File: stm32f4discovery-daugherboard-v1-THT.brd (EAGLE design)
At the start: 100 x 70 mm, 44 parts

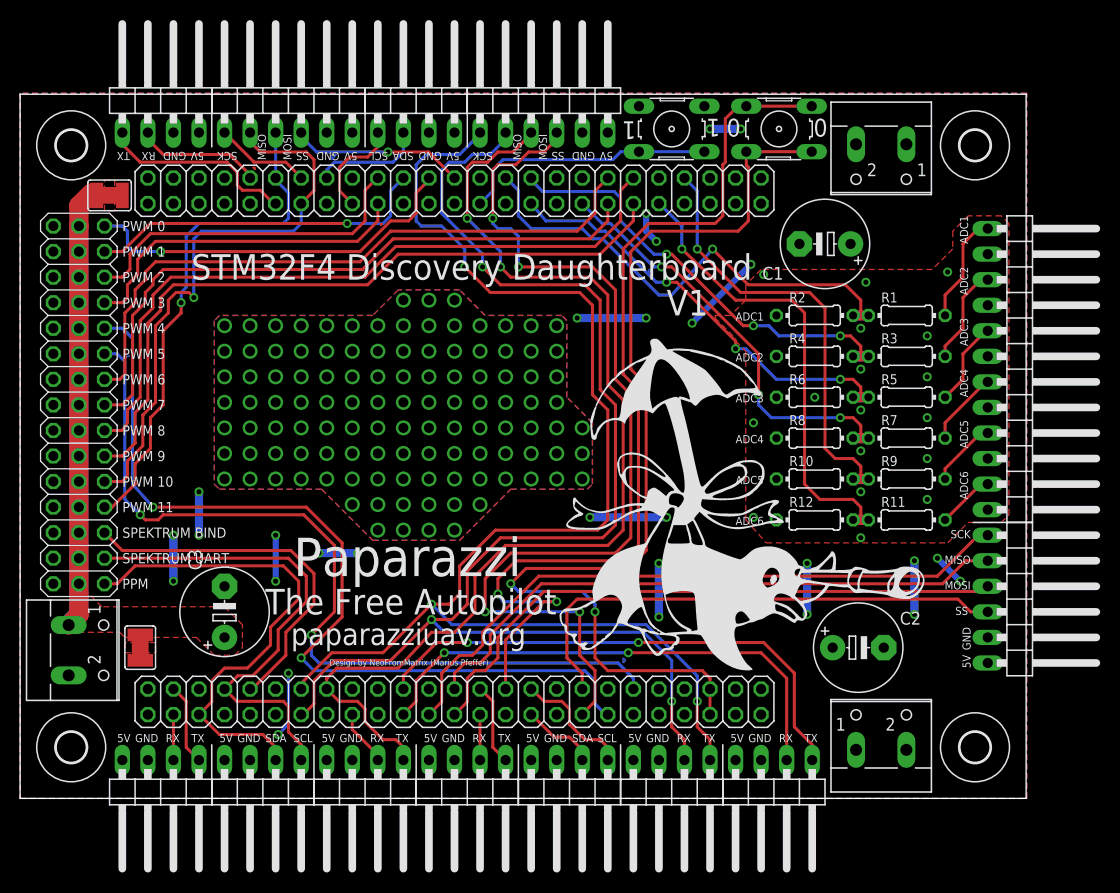
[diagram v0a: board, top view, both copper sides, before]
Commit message: all tht components, adc input protection with diodes
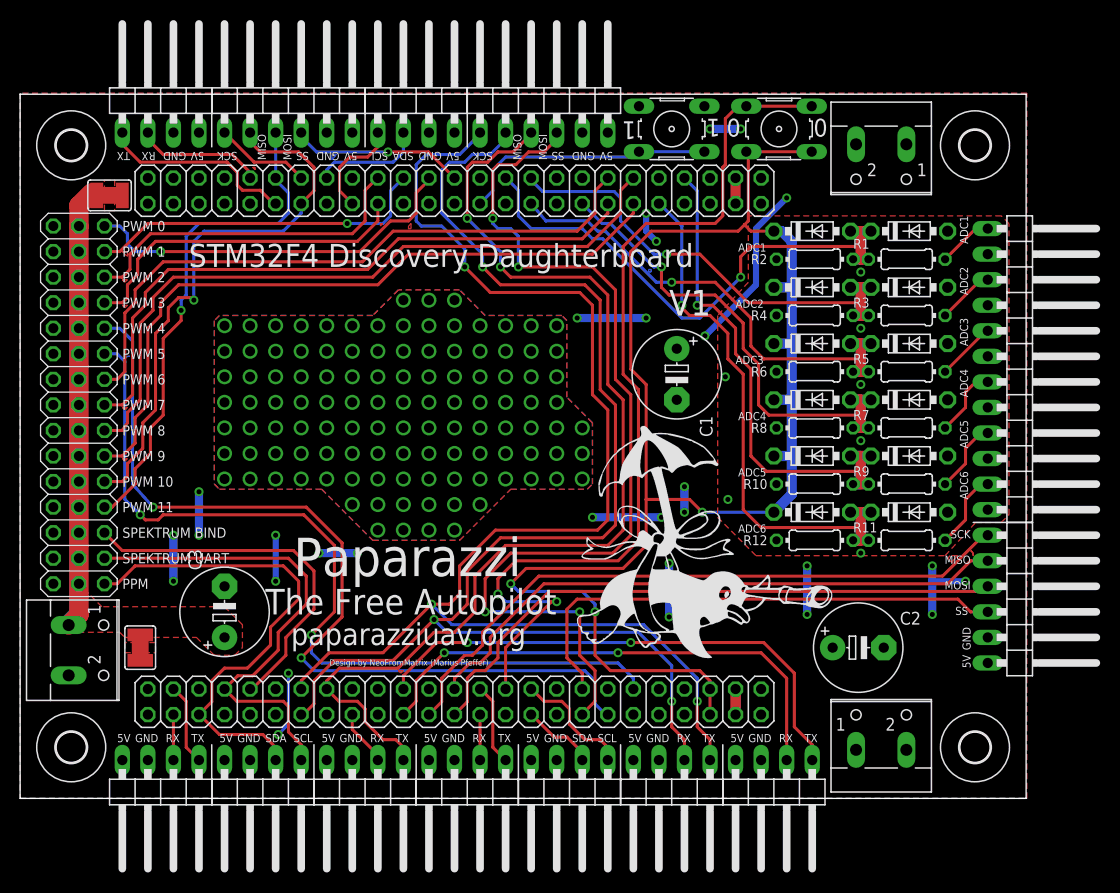
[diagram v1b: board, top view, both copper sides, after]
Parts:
- removed U$3: PAPARAZZI, paparazzi:PAPARAZZI
- added D1, D10, D11, D12, D2, D3, D4, D5, D6, D7, D8, D9: 1N4007, diode:DO41-7.6_2
- added U$4: üAüARAZZI_1400, paparazzi:PAPARAZZI_1400
- moved C1 19.6 mm to (65.3, 42.2), turned to 270 degrees
- moved R1 5.59 mm to (88.1, 53.6)
- moved R2 5.59 mm to (79.0, 53.6)
- moved R3 4.06 mm to (88.1, 48.0)
- moved R4 4.06 mm to (79.0, 48.0)
- moved R5 2.54 mm to (88.1, 42.4)
- moved R6 2.54 mm to (79.0, 42.4)
- moved R11 2.03 mm to (88.1, 25.7)
- moved R12 2.03 mm to (79.0, 25.7)
- moved R7 1.02 mm to (88.1, 36.8)
- moved R8 1.02 mm to (79.0, 36.8)
- moved R10 0.51 mm to (79.0, 31.2)
- moved R9 0.51 mm to (88.1, 31.2)
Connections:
- net 3V: now also D1.C, D11.C, D3.C, D5.C, D7.C, D9.C
- net GND: now also D10.A, D12.A, D2.A, D4.A, D6.A, D8.A
- net PA4: now also D7.A, D8.C
- net PB1: now also D1.A, D2.C
- net PC1: now also D10.C, D9.A
- net PC2: now also D11.A, D12.C
- net PC4: now also D5.A, D6.C
- net PC5: now also D3.A, D4.C
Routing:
- net 3V: track 102.0 -> 154.8 mm, vias 2 -> 3
- net PC2: track 49.6 -> 63.9 mm
- net PC1: track 46.8 -> 59.4 mm
- net PA4: track 45.6 -> 57.7 mm, vias 3 -> 1
- net PC4: track 46.4 -> 57.2 mm, vias 3 -> 1
- net PB1: track 51.9 -> 61.9 mm
- net VIN: track 71.8 -> 81.7 mm, vias 28 -> 29
- net PC5: track 46.7 -> 54.6 mm, vias 3 -> 1
- net ADC1: track 10.9 -> 5.50 mm
- net ADC2: track 9.78 -> 5.71 mm
- net N$11: track 0.00 -> 2.54 mm
- net ADC3: track 8.47 -> 5.93 mm
- net VDD: track 0.00 -> 2.54 mm
- net 5V: track 0.00 -> 2.54 mm
- net ADC6: track 5.71 -> 7.75 mm
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- added copper zone on layer 1, net N$10
- added copper zone on layer 1, net N$12
- added copper zone on layer 1, net N$13
- added copper zone on layer 1, net N$14
- added copper zone on layer 1, net N$15
- added copper zone on layer 1, net N$16
- added copper zone on layer 1, net N$17
- added copper zone on layer 1, net N$18
- added copper zone on layer 1, net N$5
- removed copper zone on layer 16, net ADC6

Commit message: input protection
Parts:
- added D13: 1N4007, diode:DO41-7.6_2
- added D14, D15: Z_DIODE_DO41-7.6, diode:DO41-7.6_Z
- moved SJ1 0.57 mm to (11.7, 14.5)
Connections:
- removed net 5V: RIGHT.3, RIGHT.4
- net GND: now also D13.A, D14.A, D15.A
- net PWM_VIN: now also D13.C
- net VIN: now also D14.C, D15.C, RIGHT.3, RIGHT.4
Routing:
- net N$11: track 2.54 -> 0.00 mm
- net 5V: track 2.54 -> 0.00 mm
- net VIN: track 81.7 -> 84.1 mm, vias 29 -> 31
- net 3V: track 154.8 -> 156.0 mm
- net PE3: track 95.7 -> 94.9 mm
- added copper zone on layer 1, net N$136
- added copper zone on layer 1, net N$19

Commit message: deleted old version, small changes in tht version
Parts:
- D14, D15: value Z_DIODE_DO41-7.6 -> 1N4007; device diode:DO41-7.6_Z -> diode:DO41-7.6_2
- moved D15 49.1 mm to (82.0, 58.9), turned to 0 degrees
- moved D14 48.0 mm to (94.0, 11.2), turned to 180 degrees
- moved C3 0.51 mm to (20.8, 18.5)
- moved U$4 0.25 mm to (54.6, 13.0)
- turned C1 to 90 degrees
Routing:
- net PB5: track 60.6 -> 59.7 mm
- net PB4: track 59.8 -> 58.9 mm
- net PB3: track 65.0 -> 64.3 mm
- net BOOT0: track 94.0 -> 94.8 mm
- net PE2: track 51.3 -> 50.6 mm
- added copper zone on layer 1, net N$137
- added copper zone on layer 16, net N$139
- added copper zone on layer 16, net N$140
- added copper zone on layer 16, net N$141
- added copper zone on layer 16, net N$142
- added copper zone on layer 16, net N$143
- added copper zone on layer 16, net N$144
